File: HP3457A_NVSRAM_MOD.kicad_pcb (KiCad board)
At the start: 2 copper layers, 17.8 x 35.6 mm, 15 parts, among them J1 Conn_01x02, U1 TC5564APL_Adapter, U2 STK12C68, U3 74AHC2G00, U4 TL431DBZ

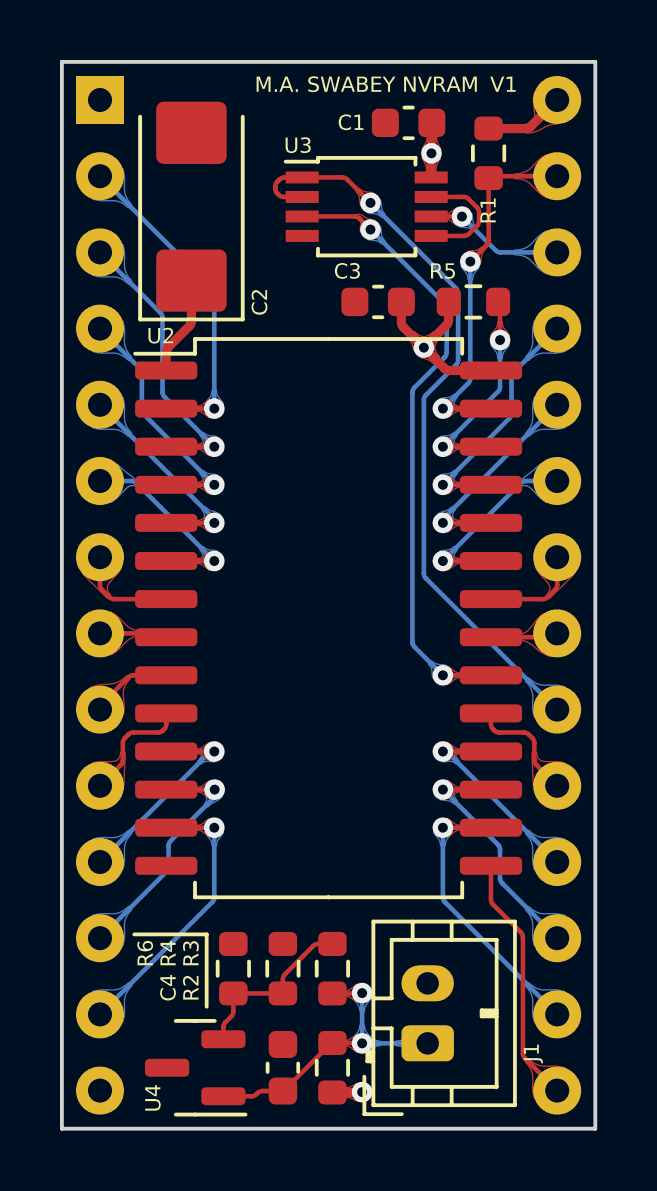
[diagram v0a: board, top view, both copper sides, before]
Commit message: Moved to 0402 resistors, tweaked pours, minor cleanups.
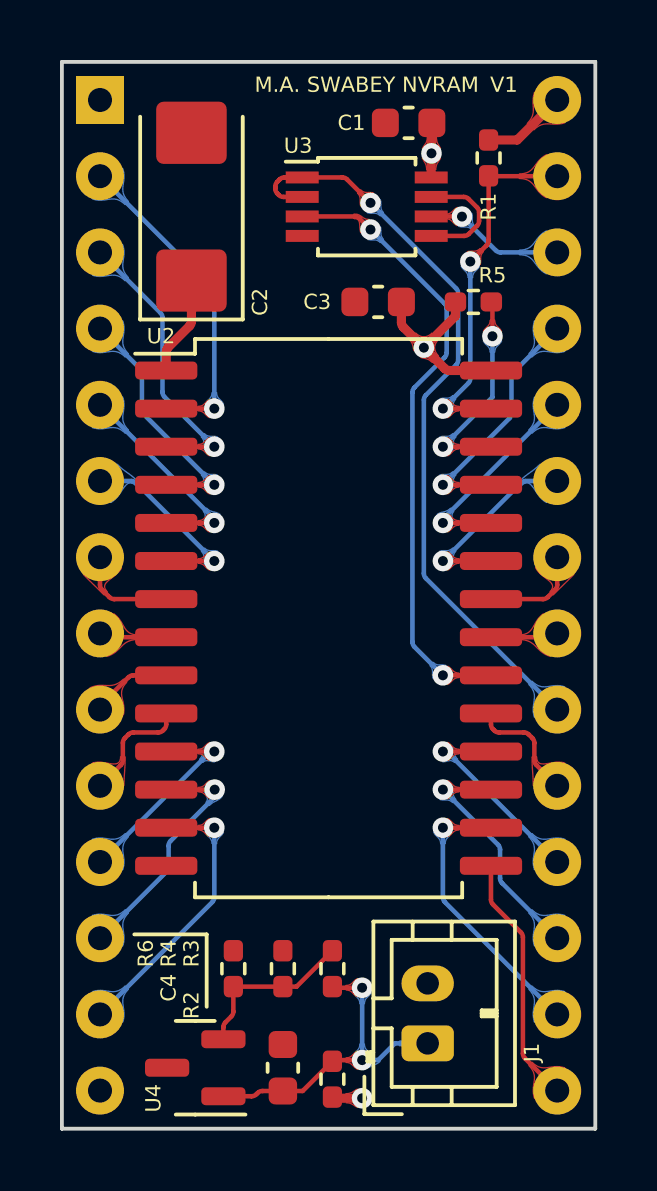
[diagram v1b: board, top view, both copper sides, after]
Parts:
- R1, R5, R6: footprint Resistor_SMD:R_0603_1608Metric -> Resistor_SMD:R_0402_1005Metric_Pad0.72x0.64mm_HandSolder
- R2: value 530 -> 150; footprint Resistor_SMD:R_0603_1608Metric -> Resistor_SMD:R_0402_1005Metric_Pad0.72x0.64mm_HandSolder
- R3: value 1.5K -> 1.3K; footprint Resistor_SMD:R_0603_1608Metric -> Resistor_SMD:R_0402_1005Metric_Pad0.72x0.64mm_HandSolder
- R4: value 3.74K -> 3.3K; footprint Resistor_SMD:R_0603_1608Metric -> Resistor_SMD:R_0402_1005Metric_Pad0.72x0.64mm_HandSolder
- moved R2 0.38 mm to (119.5, 91.1)
- moved R1 0.15 mm to (124.7, 60.4)
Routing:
- net /BATT_FAKE: track 10.3 -> 10.9 mm
- net Net-(R3-Pad2): track 5.94 -> 5.44 mm

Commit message: Design tweaked and gerbers submitted to OSHPark V1
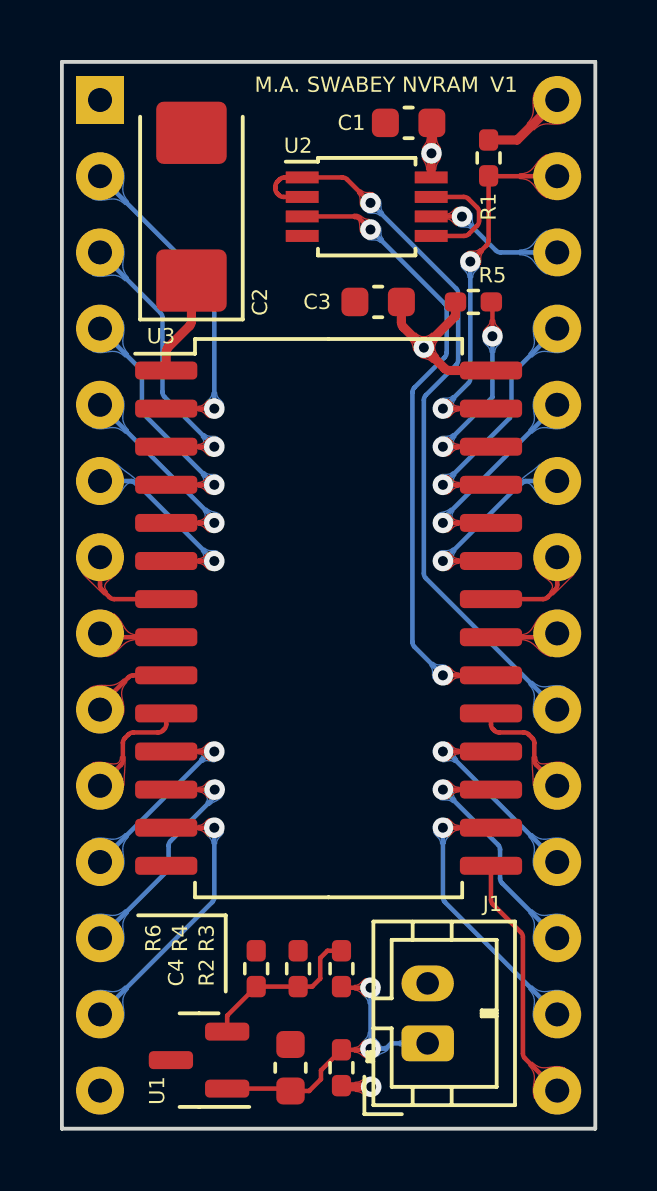
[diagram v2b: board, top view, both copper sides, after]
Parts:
- moved R6 0.76 mm to (117.0, 87.4)
- moved R4 0.51 mm to (118.4, 87.4)
- moved R2 0.49 mm to (119.8, 90.7)
- moved R3 0.30 mm to (119.8, 87.4)
- moved U1 0.28 mm to (115.1, 90.4)
- moved C4 0.25 mm to (118.1, 90.7)
- renumbered U4 to U1, U1 to U10, U3 to U2, U2 to U3

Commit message: Version submitted to OSHPark as V1
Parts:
- added C5: 22u, Capacitor_SMD:C_0603_1608Metric, F.Cu at (114.8, 61.2)
- added C6: 22u, Capacitor_SMD:C_0603_1608Metric, F.Cu at (114.8, 63.0)
- added C7: 22u, Capacitor_SMD:C_0603_1608Metric, F.Cu at (114.8, 59.4)
- C2: value 200nF -> 22u; footprint Capacitor_Tantalum_SMD:CP_EIA-6032-28_Kemet-C -> Capacitor_SMD:C_0603_1608Metric
- moved C2 2.92 mm to (114.8, 64.9), turned to 0 degrees
- moved C3 2.30 mm to (123.3, 65.4)
- moved R5 1.37 mm to (125.5, 64.6), turned to -90 degrees
- moved C1 0.31 mm to (122.0, 59.5)
- moved U2 0.31 mm to (120.7, 62.3)
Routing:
- net /VCAP: track 3.32 -> 8.03 mm
- net +5V: track 12.0 -> 15.3 mm
- net /~{WE}: track 12.2 -> 13.5 mm, vias 2 -> 3
- net GND: track 0.00 -> 1.27 mm
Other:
- board text added: "M.A. SWABEY XX62 NVSRAM"
- board text removed: "M.A. SWABEY NVRAM"

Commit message: Improved labelling and checked board in new KiCad version.
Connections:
- net +5V renamed VCC
